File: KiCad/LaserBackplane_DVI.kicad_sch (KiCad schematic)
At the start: 45 parts, among them J1 Curr. Mod., J2 DVI-I, J3 Ld+, J4 Ld-, J5 Pz+, J6 Pz-, J7 Piezo_In, K1 G6AU, Q1 MMBT3904, Q2 2N4401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

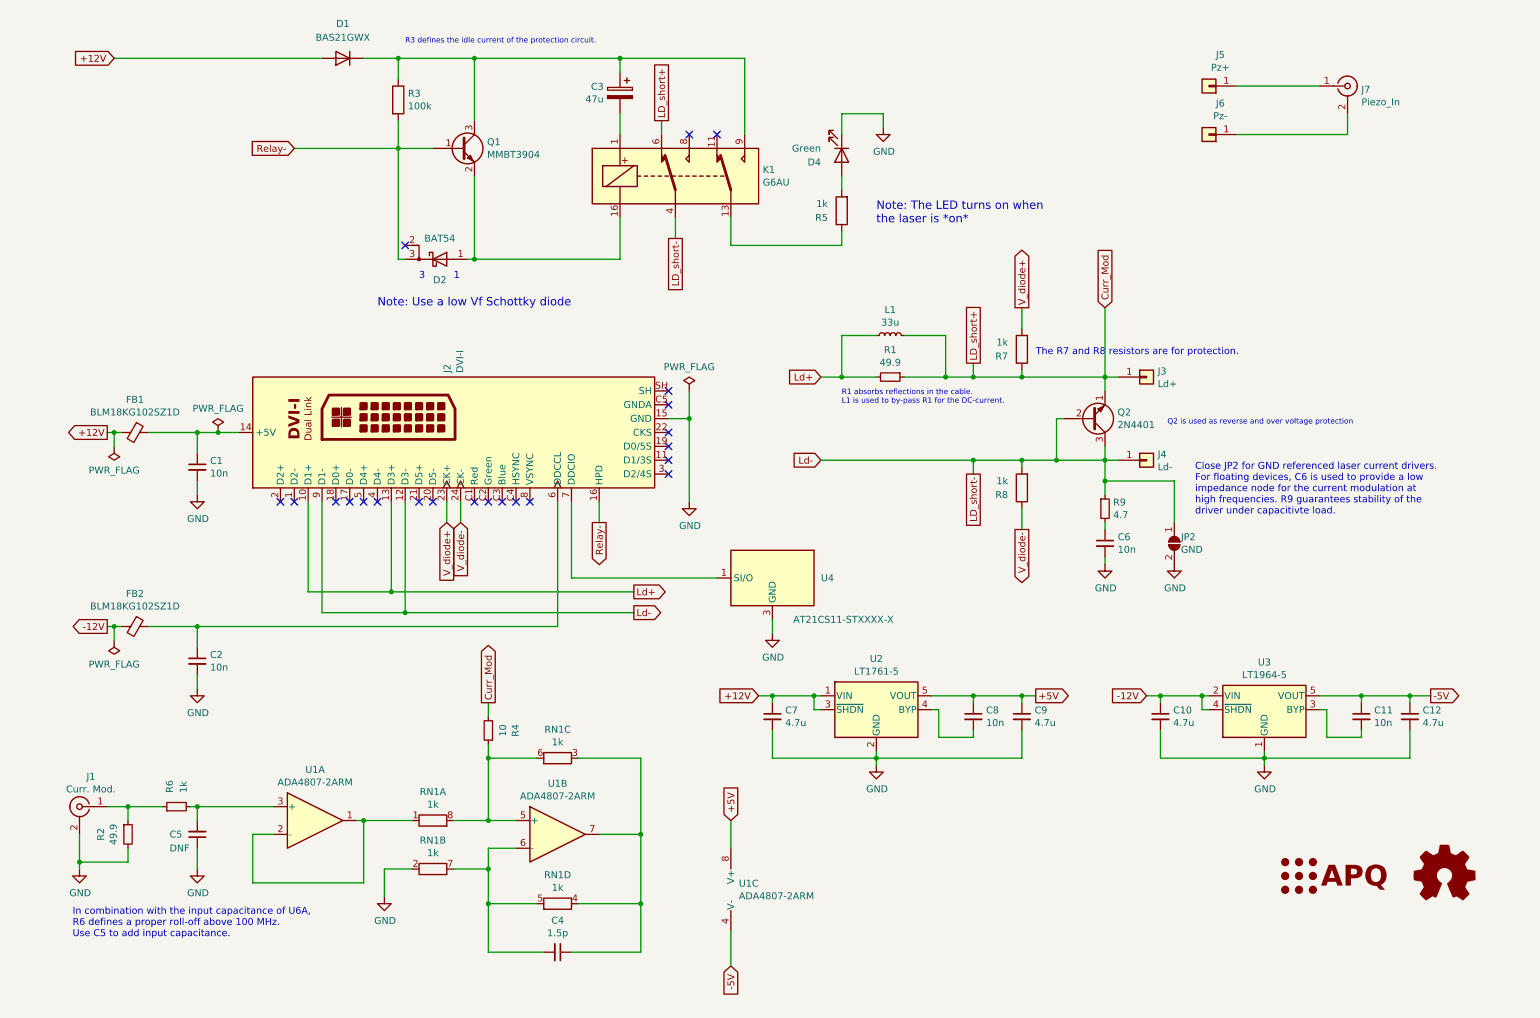
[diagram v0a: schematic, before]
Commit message: Update to KiCad 8 Removed obsolete libs and footprints
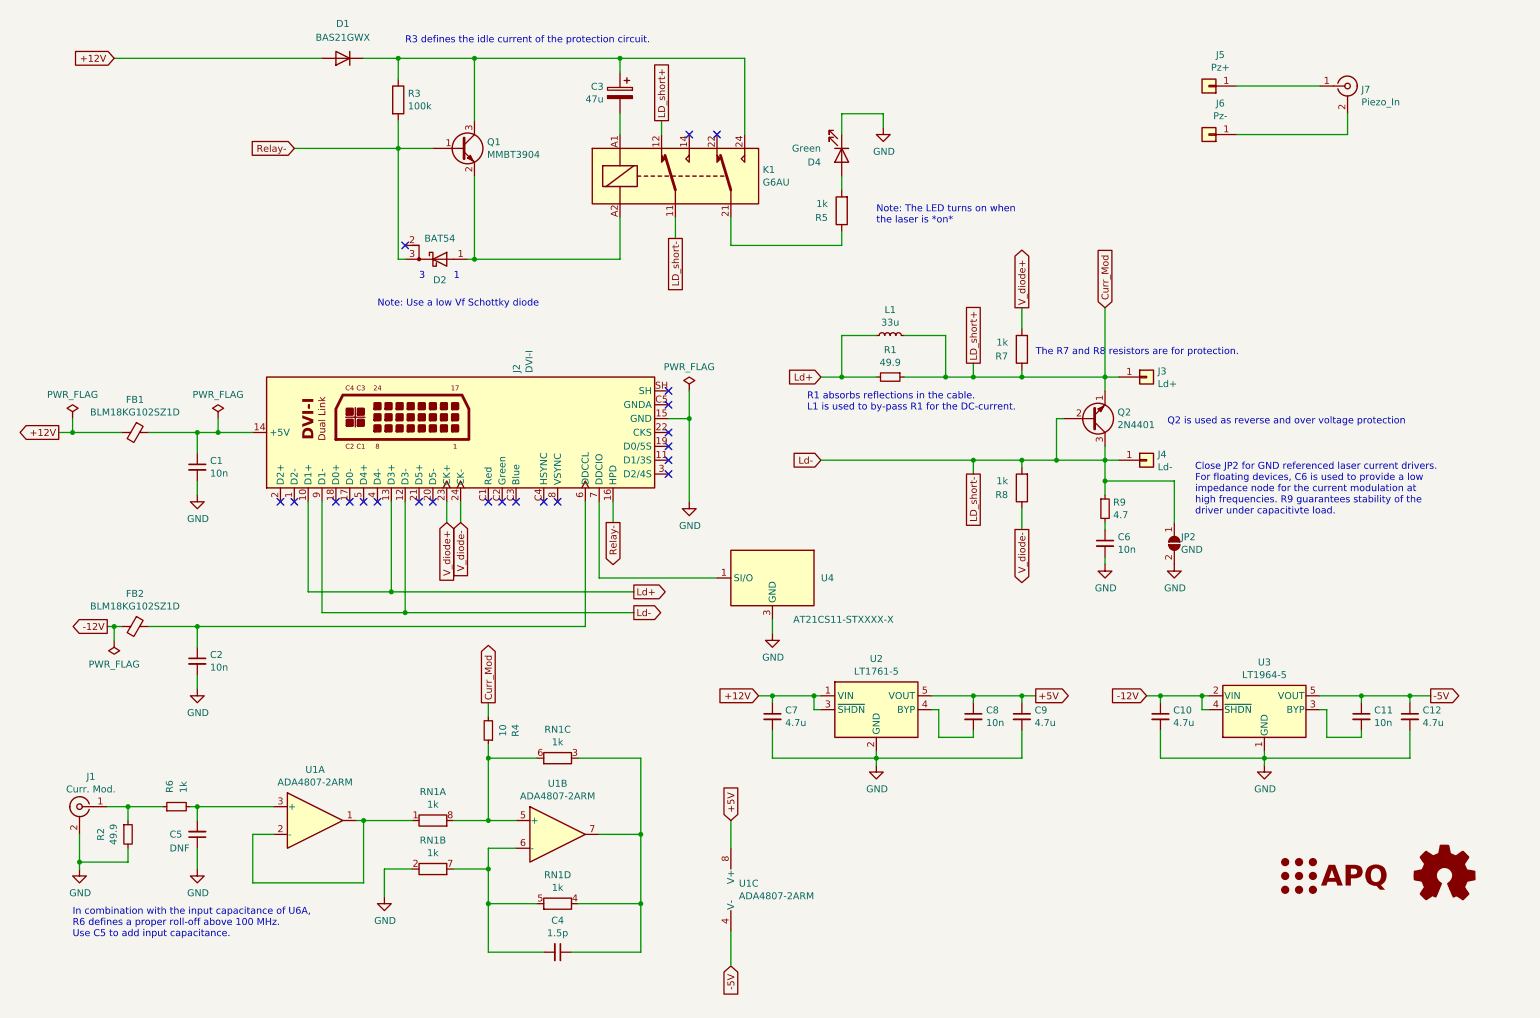
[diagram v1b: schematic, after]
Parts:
- C1, C2: MFN Kemet -> TDK; PN C0603C103K2RECAUTO -> CGA3E2X7R1H103K080AA
- C11, C6, C8: MFN Murata Electronics -> TDK; PN GRM1885C1H103JA01J -> CGA3E2X7R1H103K080AA
- J2: symbol Molex:DVI-I -> Connector:DVI-I_Dual_Link
- K1: footprint custom:Relay_SPDT_OMRON-G6A -> Relay_THT:Relay_DPDT_Omron_G6A; symbol Omron_G6AU:G6AU -> Relay:Relay_DPDT
- RN1, U1: footprint custom:MSOP-8_3x3mm_P0.65mm_mod -> Package_SO:MSOP-8_3x3mm_P0.65mm
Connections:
- net Curr_Mod: now also K1.12; no longer K1.6
- net LD_short-: now also K1.11; no longer K1.4
- net at C3.1, D1.1 (K), Q1.3 (C)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: now also K1.24; no longer K1.9
- net at C3.2: now also K1.A1; no longer K1.1
- net at D2.1 (A), Q1.2 (E): now also K1.A2; no longer K1.16
- net at R5.1: now also K1.21; no longer K1.13

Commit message: Updated symbols
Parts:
- Q2: MFN ON Semiconductor -> onsemi
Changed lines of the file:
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@@
 			)
 		)
-		(property "Description" ""
+		(property "Description" "Polarized capacitor"
 			(at 124.46 30.48 0)
 			(effects
@@
 			)
 		)
-		(property "Datasheet" ""
+		(property "Datasheet" "~"
 			(at 83.82 31.75 0)
 			(effects
@@
 			)
 		)
-		(property "Description" ""
+		(property "Description" "Resistor"
 			(at 83.82 31.75 0)
 			(effects
@@
 			)
 		)
-		(property "Description" ""
+		(property "Description" "Resistor"
 			(at 165.1 52.07 0)
 			(effects
@@
 			)
 		)
-		(property "Description" ""
+		(property "Description" "Light emitting diode"
 			(at 165.1 41.91 0)
 			(effects
@@
 			)
 		)
-		(property "Description" ""
+		(property "Description" "Diode"
 			(at 73.66 24.13 0)
 			(effects
@@
 			)
 		)
-		(property "Description" ""
+		(property "Description" "Resistor, small symbol"
 			(at 34.29 166.37 0)
 			(effects
@@
 			)
 		)
-		(property "Description" ""
+		(property "Description" "0.2A Ic, 40V Vce, Small Signal NPN Transistor, SOT-23"
 			(at 95.25 40.64 0)
 			(effects
@@
 			)
 		)
-		(property "Description" ""
+		(property "Description" "Resistor, small symbol"
 			(at 173.99 82.55 0)
 			(effects
@@
 			)
 		)
-		(property "Description" ""
+		(property "Description" "Generic connector, single row, 01x01, script generated (kicad-library-utils/schlib/autogen/connector/)"
 			(at 232.41 29.21 0)
 			(effects
@@
 			)
 		)
-		(property "Description" ""
+		(property "Description" "Generic connector, single row, 01x01, script generated (kicad-library-utils/schlib/autogen/connector/)"
 			(at 232.41 38.1 0)
 			(effects
@@
 			)
 		)
-		(property "Description" ""
+		(property "Description" "Generic connector, single row, 01x01, script generated (kicad-library-utils/schlib/autogen/connector/)"
 			(at 220.98 82.55 0)
 			(effects
@@
 			)
 		)
-		(property "Description" ""
+		(property "Description" "Generic connector, single row, 01x01, script generated (kicad-library-utils/schlib/autogen/connector/)"
 			(at 220.98 97.79 0)
 			(effects
@@
 			)
 		)
-		(property "Description" ""
+		(property "Description" "NPN transistor, emitter/base/collector"
 			(at 210.82 90.17 0)
 			(effects
@@
 			)
 		)
-		(property "MFN" "ON Semiconductor"
+		(property "MFN" "onsemi"
 			(at 210.82 90.17 0)
 			(effects
@@
 			)
 		)
-		(property "Description" ""
+		(property "Description" "Open Hardware logo, small"
 			(at 275.59 173.99 0)
 			(effects
@@
 			)
 		)
+		(property "Sim.Enable" "0"
+			(at 275.59 173.99 0)
+			(effects
+				(font
+					(size 1.27 1.27)
+				)
+				(hide yes)
+			)
+		)
 		(instances
 			(project "LaserBackplane_DVI"
@@
 			)
 		)
-		(property "Description" ""
+		(property "Description" "Atoms - Photons - Quanta"
 			(at 241.3 173.99 0)
 			(effects
@@
 			)
 		)
+		(property "Sim.Enable" "0"
+			(at 241.3 173.99 0)
+			(effects
+				(font
+					(size 1.27 1.27)
+				)
+				(hide yes)
+			)
+		)
 		(instances
 			(project "LaserBackplane_DVI"
@@
 			)
 		)
-		(property "Description" ""
+		(property "Description" "Resistor"
 			(at 198.12 77.47 0)
 			(effects
@@
 			)
 		)
-		(property "Description" ""
+		(property "Description" "Resistor"
 			(at 198.12 102.87 0)
 			(effects
@@
 			)
 		)
-		(property "Description" ""
+		(property "Description" "Unpolarized capacitor, small symbol"
 			(at 46.99 99.06 0)
 			(effects
@@
 			)
 		)
-		(property "Description" ""
+		(property "Description" "Ferrite bead, small symbol"
 			(at 35.56 92.71 0)
 			(effects
@@
 			)
 		)
-		(property "Description" ""
+		(property "Description" "Unpolarized capacitor, small symbol"
 			(at 46.99 134.62 0)
 			(effects
@@
 			)
 		)
-		(property "Description" ""
+		(property "Description" "Ferrite bead, small symbol"
 			(at 35.56 128.27 0)
 			(effects
@@
 			)
 		)
-		(property "Description" ""
+		(property "Description" "Inductor, small symbol"
 			(at 173.99 74.93 0)
 			(effects
@@
 			)
 		)
-		(property "Description" ""
+		(property "Description" "Unpolarized capacitor, small symbol"
 			(at 189.23 144.78 0)
 			(effects
@@
 			)
 		)
-		(property "Description" ""
+		(property "Description" "Unpolarized capacitor, small symbol"
 			(at 152.4 144.78 0)
 			(effects
@@
 			)
 		)
-		(property "Description" ""
+		(property "Description" "Unpolarized capacitor, small symbol"
 			(at 198.12 144.78 0)
 			(effects
@@
 			)
 		)
-		(property "Description" ""
+		(property "Description" "Unpolarized capacitor, small symbol"
 			(at 260.35 144.78 0)
 			(effects
@@
 			)
 		)
-		(property "Description" ""
+		(property "Description" "Unpolarized capacitor, small symbol"
 			(at 223.52 144.78 0)
 			(effects
@@
 			)
 		)
-		(property "Description" ""
+		(property "Description" "Unpolarized capacitor, small symbol"
 			(at 269.24 144.78 0)
 			(effects
@@
 			)
 		)
-		(property "Description" ""
+		(property "Description" "MICROPOWER 200mA Low Noise LDO negative regulator, fixed output -5V, TSOT-23-5"
 			(at 242.57 143.51 0)
 			(effects
@@
 	)
 	(symbol
-		(lib_name "ADA4807-2ARM_2")
 		(lib_id "Amplifier_Operational:ADA4807-2ARM")
 		(at 68.58 163.83 0)
@@
 			)
 		)
-		(property "Description" ""
+		(property "Description" "Dual Rail-to-Rail Input/Output Amplifiers, MSOP-8"
 			(at 68.58 163.83 0)
 			(effects
@@
 	)
 	(symbol
-		(lib_name "ADA4807-2ARM_1")
 		(lib_id "Amplifier_Operational:ADA4807-2ARM")
 		(at 113.03 166.37 0)
@@
 			)
 		)
-		(property "Description" ""
+		(property "Description" "Dual Rail-to-Rail Input/Output Amplifiers, MSOP-8"
 			(at 113.03 166.37 0)
 			(effects
@@
 			)
 		)
-		(property "Description" ""
+		(property "Description" "Unpolarized capacitor, small symbol"
 			(at 113.03 187.96 0)
 			(effects
@@
 			)
 		)
-		(property "Description" ""
+		(property "Description" "Dual Rail-to-Rail Input/Output Amplifiers, MSOP-8"
 			(at 147.32 176.53 0)
 			(effects
@@
 			)
 		)
-		(property "Description" ""
+		(property "Description" "Resistor, small symbol"
 			(at 100.33 147.32 0)
 			(effects
@@
 			)
 		)
-		(property "Description" ""
+		(property "Description" "I2C Serial EEPROM, 1Kb (128x8) with Unique Serial Number, SOT-23"
 			(at 152.4 119.38 0)
 			(effects
@@
 			)
 		)
-		(property "Description" ""
+		(property "Description" "Solder Jumper, 2-pole, open"
 			(at 226.06 113.03 0)
 			(effects
@@
 			)
 		)
-		(property "Description" ""
+		(property "Description" "Resistor, small symbol"
 			(at 213.36 106.68 0)
 			(effects
@@
 			)
 		)
-		(property "Description" ""
+		(property "Description" "Unpolarized capacitor, small symbol"
 			(at 46.99 166.37 0)
 			(effects
@@
 			)
 		)
-		(property "Description" ""
+		(property "Description" "Resistor, small symbol"
 			(at 43.18 161.29 0)
 			(effects
@@
 			)
 		)
-		(property "Description" ""
+		(property "Description" "Unpolarized capacitor, small symbol"
 			(at 213.36 113.03 0)
 			(effects

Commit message: Replaced EOL parts
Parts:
- C3: MFN Nichicon -> Würth Elektronik; PN UHV1V470MDD -> 860040572002
- C5: now not fitted
- R3: MFN Susumu -> Vishay; PN RR0816P-104-D -> CRCW0603100KFKEA
- R5, R6, R7, R8: PN RR0816P-102-D -> RG1608P-102-D-T5
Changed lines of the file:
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@@
 			)
 		)
-		(property "MFN" "Nichicon"
+		(property "MFN" "Würth Elektronik"
 			(at 124.46 30.48 0)
 			(effects
@@
 			)
 		)
-		(property "PN" "UHV1V470MDD"
+		(property "PN" "860040572002"
 			(at 124.46 30.48 0)
 			(effects
@@
 			)
 		)
-		(property "MFN" "Susumu"
+		(property "MFN" "Vishay"
 			(at 83.82 31.75 0)
 			(effects
@@
 			)
 		)
-		(property "PN" "RR0816P-104-D"
+		(property "PN" "CRCW0603100KFKEA"
 			(at 83.82 31.75 0)
 			(effects
@@
 			)
 		)
-		(property "PN" "RR0816P-102-D"
+		(property "PN" "RG1608P-102-D-T5"
 			(at 165.1 52.07 0)
 			(effects
@@
 			)
 		)
-		(property "PN" "RR0816P-102-D"
+		(property "PN" "RG1608P-102-D-T5"
 			(at 198.12 77.47 0)
 			(effects
@@
 			)
 		)
-		(property "PN" "RR0816P-102-D"
+		(property "PN" "RG1608P-102-D-T5"
 			(at 198.12 102.87 0)
 			(effects
@@
 		(in_bom yes)
 		(on_board yes)
-		(dnp no)
+		(dnp yes)
 		(property "Reference" "C5"
 			(at 41.91 166.37 0)
@@
 			)
 		)
+		(property "MFN" ""
+			(at 46.99 166.37 0)
+			(effects
+				(font
+					(size 1.27 1.27)
+				)
+				(hide yes)
+			)
+		)
+		(property "PN" ""
+			(at 46.99 166.37 0)
+			(effects
+				(font
+					(size 1.27 1.27)
+				)
+				(hide yes)
+			)
+		)
 		(pin "1"
 		)
@@
 			)
 		)
-		(property "PN" "RR0816P-102-D"
+		(property "PN" "RG1608P-102-D-T5"
 			(at 43.18 161.29 0)
 			(effects
